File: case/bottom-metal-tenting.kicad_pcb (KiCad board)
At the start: 2 copper layers, 148 x 99.1 mm, 9 parts

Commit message: update case files
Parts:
- removed the REF** at (197.8, 144.5)
- removed the REF** at (74.5, 67.5)
- removed the REF** at (74.5, 119.5)
- removed the REF** at (210.5, 64.0)
- added REF**: MountingHole_4.5mm, MountingHole:MountingHole_4.5mm, F.Cu at (217.7, 58.0)
- added REF**: MountingHole_4.5mm, MountingHole:MountingHole_4.5mm, F.Cu at (205.1, 142.4)
- added REF**: MountingHole_4.5mm, MountingHole:MountingHole_4.5mm, F.Cu at (81.7, 64.0)
- added REF**: MountingHole_4.5mm, MountingHole:MountingHole_4.5mm, F.Cu at (81.7, 117.0)
- moved H1 7.83 mm to (114.8, 71.5)
- moved H2 7.83 mm to (185.8, 120.0)
- moved H3 7.83 mm to (94.8, 90.5)
- moved H4 7.83 mm to (134.2, 106.0)
- moved H5 7.83 mm to (172.2, 74.0)
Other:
- board size 148 x 99.1 mm -> 148 x 100.4 mm

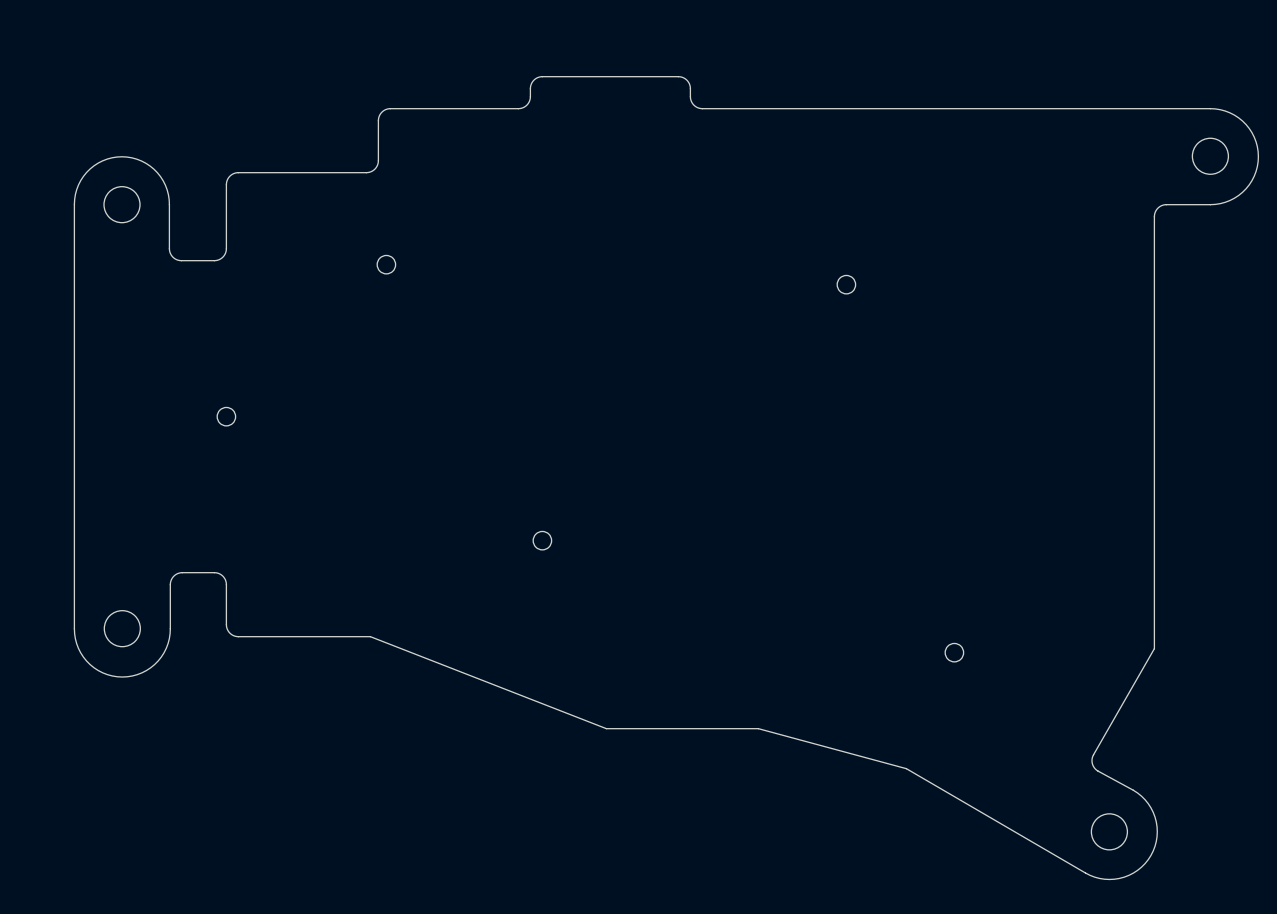
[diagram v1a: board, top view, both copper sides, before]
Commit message: update cases, extra hole on right side
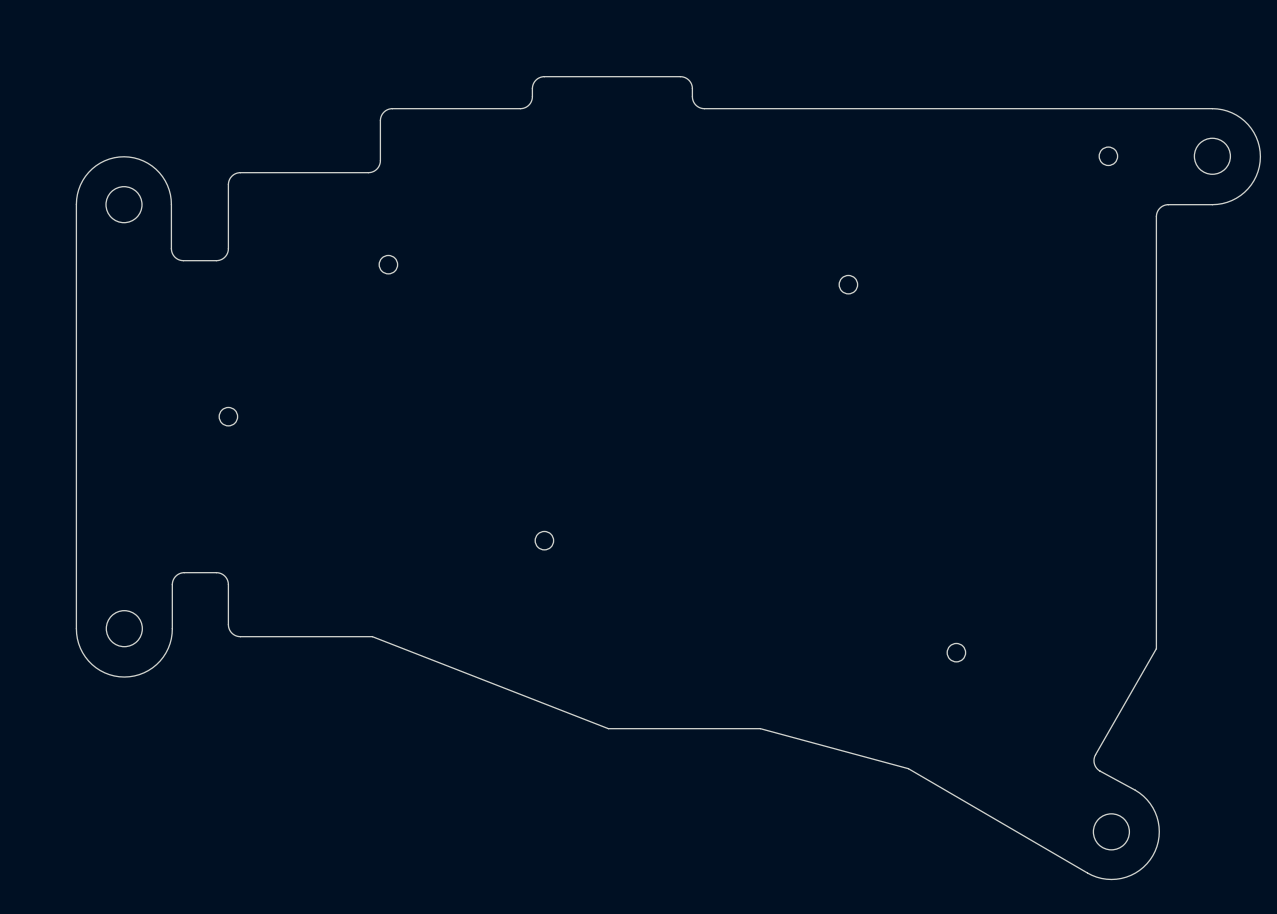
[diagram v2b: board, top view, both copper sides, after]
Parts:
- added H5: MountingHole, kbd:thread_m2, F.Cu at (205.0, 58.0)
- moved REF** 0.25 mm to (205.4, 142.4)
- moved REF** 0.25 mm to (82.0, 117.0)
- moved H1 0.25 mm to (115.0, 71.5)
- moved H2 0.25 mm to (186.0, 120.0)
- moved H3 0.25 mm to (95.0, 90.5)
- moved H4 0.25 mm to (134.5, 106.0)
- moved H5 0.25 mm to (172.5, 74.0)
- moved REF** 0.25 mm to (218.0, 58.0)
- moved REF** 0.25 mm to (82.0, 64.0)

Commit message: update case files
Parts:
- removed the H5 at (172.5, 74.0)
- removed the H5 at (205.0, 58.0)
- added H5: MountingHole, kbd:thread_m2, F.Cu at (174.0, 69.5)
- added H6: MountingHole, kbd:thread_m2, F.Cu at (196.5, 76.5)
- added H7: MountingHole, kbd:thread_m2, F.Cu at (205.2, 76.5)
- moved REF** 15.9 mm to (206.5, 47.0), turned to 90 degrees
- moved REF** 4.95 mm to (206.4, 137.6)
- moved H2 4.79 mm to (187.5, 115.5)
- moved H4 4.79 mm to (136.0, 101.5)
- moved H1 4.55 mm to (114.8, 67.0)
- moved REF** 3.92 mm to (80.1, 67.5), turned to 95 degrees
- moved REF** 3.80 mm to (84.9, 119.5), turned to -85 degrees
- moved H3 2.71 mm to (95.2, 93.2), turned to 5 degrees
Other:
- board size 148 x 100.4 mm -> 139.1 x 102.6 mm

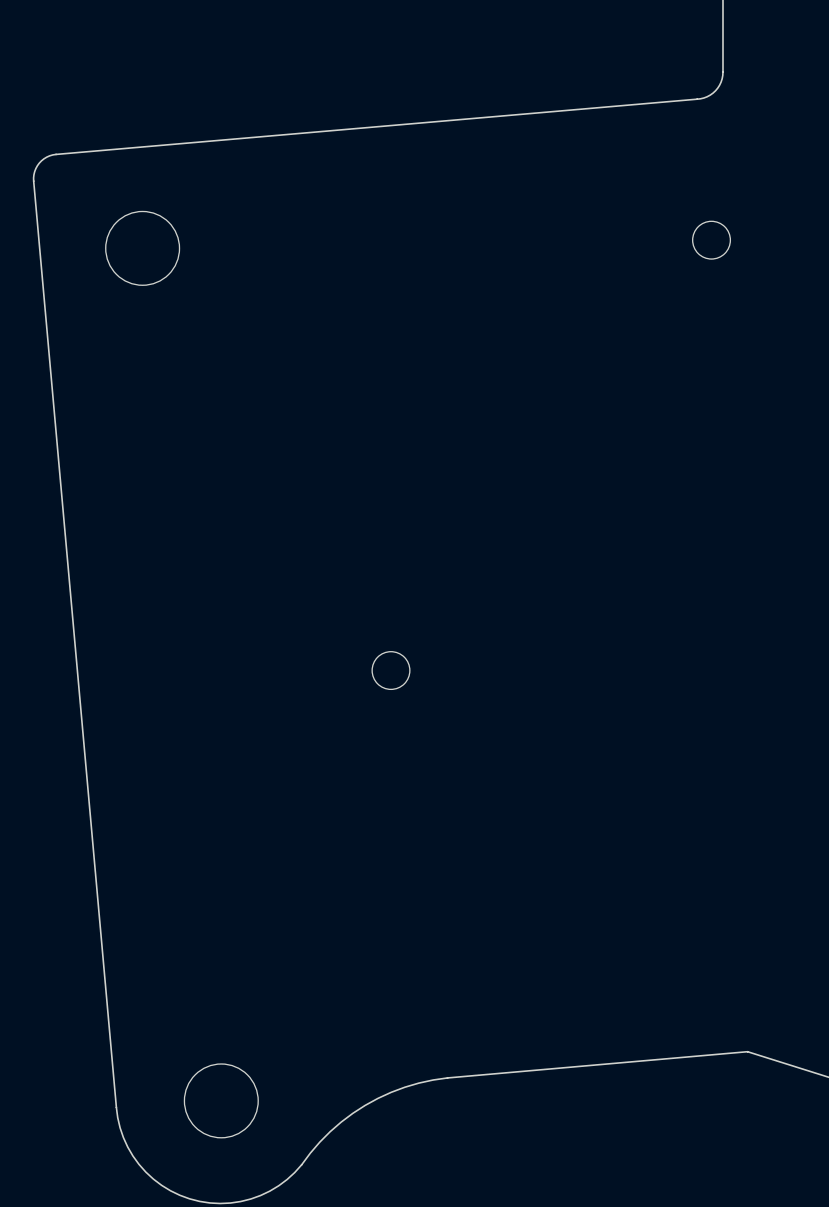
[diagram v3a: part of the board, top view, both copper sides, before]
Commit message: update bottom-tenting
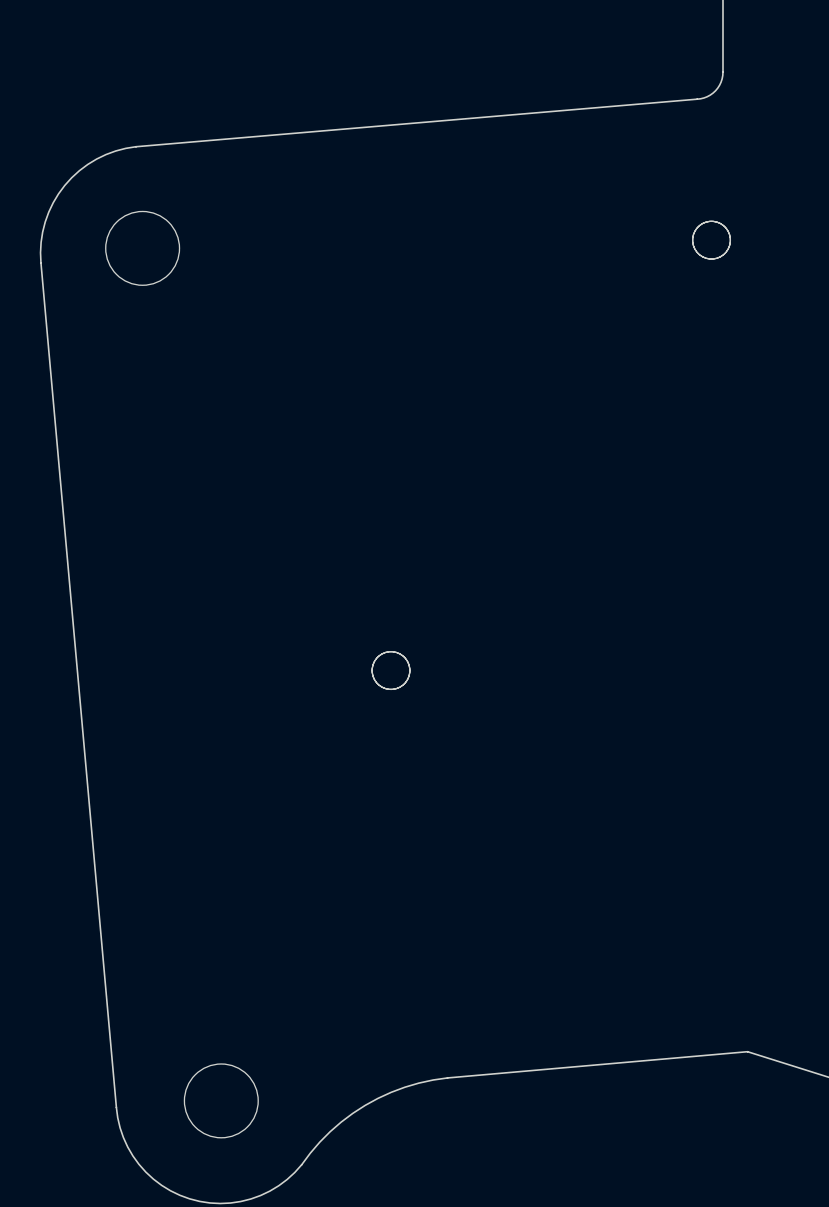
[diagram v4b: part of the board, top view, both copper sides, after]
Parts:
- added H1: MountingHole, kbd:thread_m2, F.Cu at (114.8, 67.0)
- added H3: MountingHole, kbd:thread_m2, F.Cu at (95.2, 93.2)
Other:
- board size 139.1 x 102.6 mm -> 138.7 x 102.6 mm
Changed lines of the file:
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@@
+    (pad "" np_thru_hole circle locked (at 0 0) (size 2.3 2.3) (drill 2.3) (layers *.Cu *.Mask))
+  )
+  (footprint "kbd:thread_m2" (layer "F.Cu")
+    (at 114.8 67)
+    (descr "Mounting Hole 2.2mm, no annular, M2")
+    (tags "mounting hole 2.2mm no annular m2")
+    (property "Sheetfile" "full.kicad_sch")
+    (property "Sheetname" "")
+    (attr exclude_from_pos_files exclude_from_bom)
+    (fp_text reference "H1" (at -0.95 -0.55) (layer "F.Fab") hide
+      (effects (font (size 1 1) (thickness 0.15)))
+    )
+    (fp_text value "MountingHole" (at 0 0.55) (layer "F.Fab") hide
+      (effects (font (size 1 1) (thickness 0.15)))
+    )
     (pad "" np_thru_hole circle locked (at 0 0) (size 2.3 2.3) (drill 2.3) (layers *.Cu *.Mask))
   )
@@
     (pad "" np_thru_hole circle locked (at 0 0 5) (size 2.3 2.3) (drill 2.3) (layers *.Cu *.Mask))
   )
+  (footprint "kbd:thread_m2" (layer "F.Cu")
+    (at 95.25 93.25 5)
+    (descr "Mounting Hole 2.2mm, no annular, M2")
+    (tags "mounting hole 2.2mm no annular m2")
+    (property "Sheetfile" "full.kicad_sch")
+    (property "Sheetname" "")
+    (attr exclude_from_pos_files exclude_from_bom)
+    (fp_text reference "H3" (at -0.95 -0.55 5) (layer "F.Fab") hide
+      (effects (font (size 1 1) (thickness 0.15)))
+    )
+    (fp_text value "MountingHole" (at 0 0.55 5) (layer "F.Fab") hide
+      (effects (font (size 1 1) (thickness 0.15)))
+    )
+    (pad "" np_thru_hole circle locked (at 0 0 5) (size 2.3 2.3) (drill 2.3) (layers *.Cu *.Mask))
+  )
   (gr_arc (start 175 50) (mid 174.098612 49.727082) (end 173.5 49) (layer "Edge.Cuts") (width 0.1))
-  (gr_line (start 98.7 118.1) (end 117 116.5) (layer "Edge.Cuts") (width 0.1))
-  (gr_line (start 73.454724 63.394872) (end 78.5 119.9) (layer "Edge.Cuts") (width 0.1))
-  (gr_arc (start 73.454724 63.394872) (mid 73.8 62.3) (end 74.818282 61.769846) (layer "Edge.Cuts") (width 0.1))
+  (gr_line (start 73.9 68.4) (end 78.5 119.9) (layer "Edge.Cuts") (width 0.1))
   (gr_line (start 212.549038 46.999998) (end 212.5 115) (layer "Edge.Cuts") (width 0.1))
   (gr_line (start 163 125) (end 144 125) (layer "Edge.Cuts") (width 0.1))
   (gr_arc (start 209.400001 132.403849) (mid 211.587178 140.566506) (end 203.42452 142.753686) (layer "Edge.Cuts") (width 0.1))
   (gr_arc (start 200.5 51) (mid 200.06066 52.06066) (end 199 52.5) (layer "Edge.Cuts") (width 0.1))
-  (gr_line (start 115.5 49) (end 115.5 56.75) (layer "Edge.Cuts") (width 0.1))
   (gr_line (start 117 47.5) (end 133 47.5) (layer "Edge.Cuts") (width 0.1))
-  (gr_line (start 113.925797 58.400232) (end 74.818282 61.769846) (layer "Edge.Cuts") (width 0.1))
+  (gr_line (start 113.925797 58.400232) (end 79.7 61.3) (layer "Edge.Cuts") (width 0.1))
   (gr_arc (start 115.5 49) (mid 115.939369 47.939369) (end 117 47.5) (layer "Edge.Cuts") (width 0.1))
   (gr_arc (start 134.5 45) (mid 134.939369 43.939369) (end 136 43.5) (layer "Edge.Cuts") (width 0.1))
@@
   (gr_line (start 134.5 45) (end 134.5 46) (layer "Edge.Cuts") (width 0.1))
   (gr_arc (start 89.8 123.4) (mid 93.670568 119.777002) (end 98.7 118.1) (layer "Edge.Cuts") (width 0.1))
+  (gr_arc (start 115.5 56.75) (mid 115.043319 57.890314) (end 113.925797 58.400232) (layer "Edge.Cuts") (width 0.1))
+  (gr_line (start 115.5 49) (end 115.5 56.75) (layer "Edge.Cuts") (width 0.1))
   (gr_arc (start 200.549036 47.000002) (mid 206.549038 40.999996) (end 212.549038 46.999998) (layer "Edge.Cuts") (width 0.1))
+  (gr_line (start 98.7 118.1) (end 117 116.5) (layer "Edge.Cuts") (width 0.1))
   (gr_arc (start 172 48) (mid 172.901388 48.272918) (end 173.5 49) (layer "Edge.Cuts") (width 0.1))
   (gr_line (start 154.5 46.5) (end 154.5 45) (layer "Edge.Cuts") (width 0.1))
@@
   (gr_line (start 200.549036 47.000002) (end 200.5 51) (layer "Edge.Cuts") (width 0.1))
   (gr_arc (start 89.8 123.4) (mid 82.965665 125.473708) (end 78.5 119.9) (layer "Edge.Cuts") (width 0.1))
-  (gr_arc (start 115.5 56.75) (mid 115.043319 57.890314) (end 113.925797 58.400232) (layer "Edge.Cuts") (width 0.1))
   (gr_line (start 204.979662 128.1) (end 212.5 115) (layer "Edge.Cuts") (width 0.1))
+  (gr_arc (start 73.9 68.4) (mid 75.349279 63.664904) (end 79.7 61.3) (layer "Edge.Cuts") (width 0.1))
   (gr_arc (start 153 43.5) (mid 154.06066 43.93934) (end 154.5 45) (layer "Edge.Cuts") (width 0.1))
   (gr_line (start 175 50) (end 191 50) (layer "Edge.Cuts") (width 0.1))

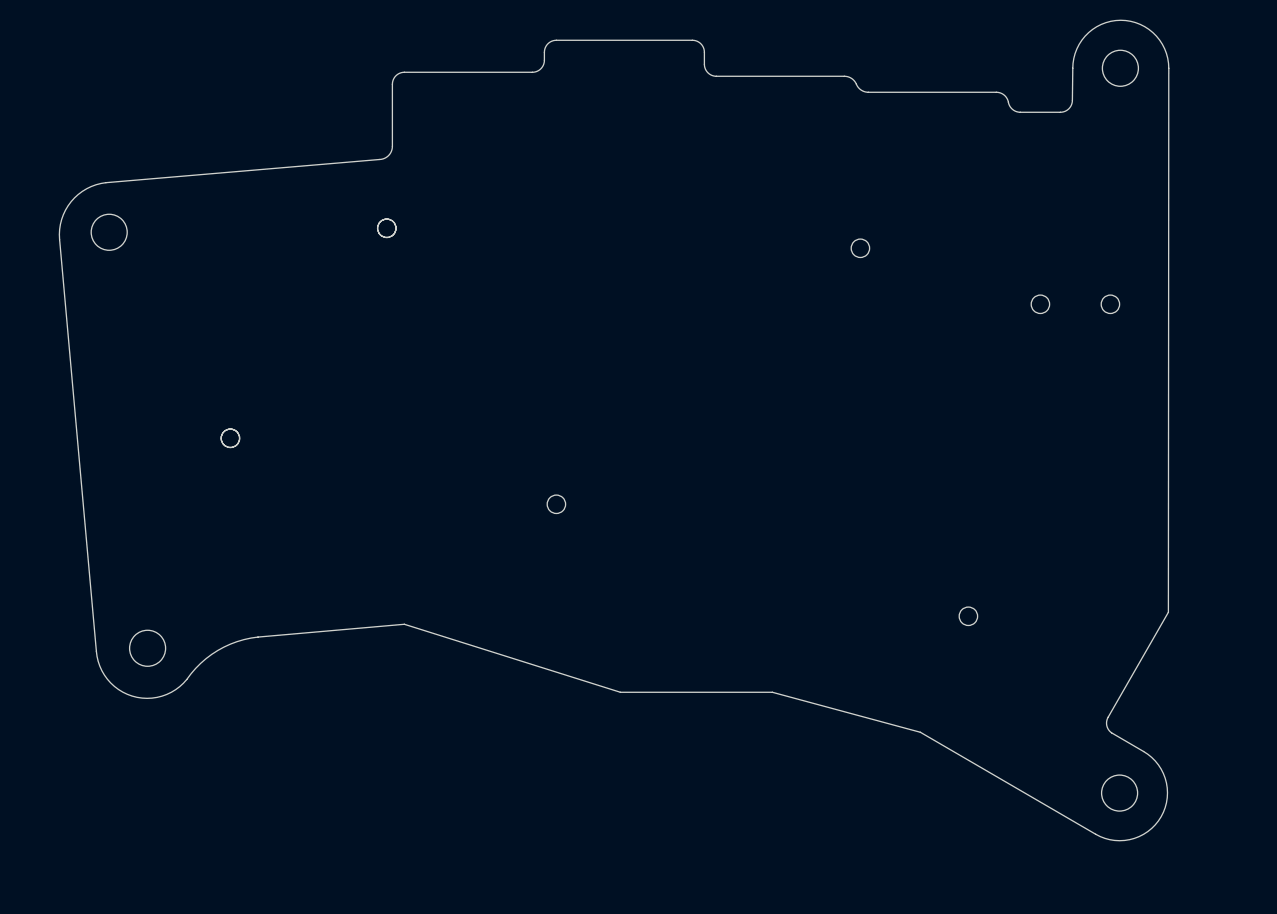
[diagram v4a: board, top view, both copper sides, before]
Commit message: fix dxf files
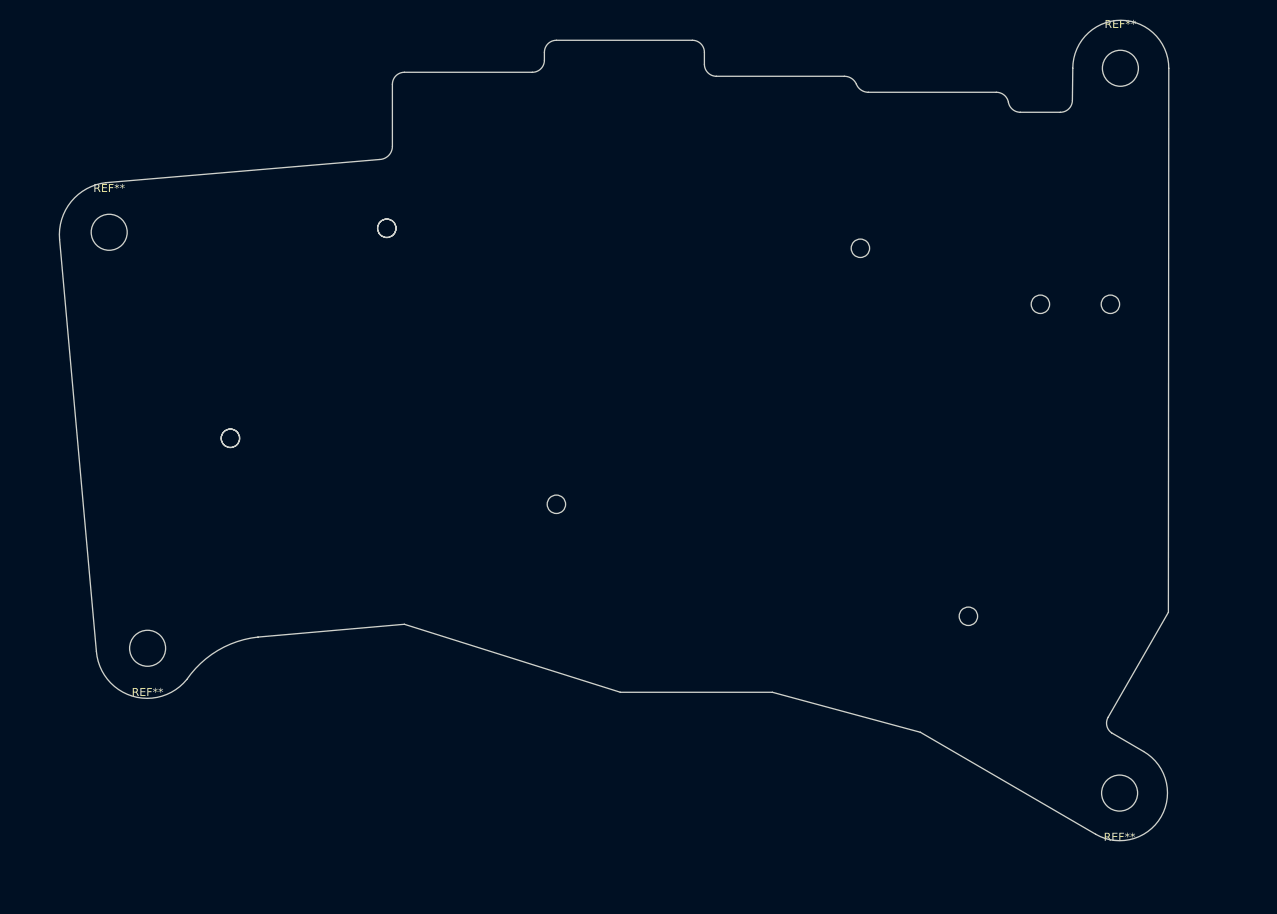
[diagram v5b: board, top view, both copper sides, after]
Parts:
- H1 (x2), H2, H3 (x2), H4, H5, H6, H7: footprint kbd:thread_m2 -> pica:thread_m2_hole
- REF** (x4): footprint MountingHole:MountingHole_4.5mm -> pica:MountingHole_4.5mm
- turned REF** to 0 degrees (x2)
- turned REF** to 180 degrees (x2)
